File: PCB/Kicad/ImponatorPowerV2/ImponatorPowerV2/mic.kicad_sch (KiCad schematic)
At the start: 13 parts, among them U5 MAX4466EXK+T

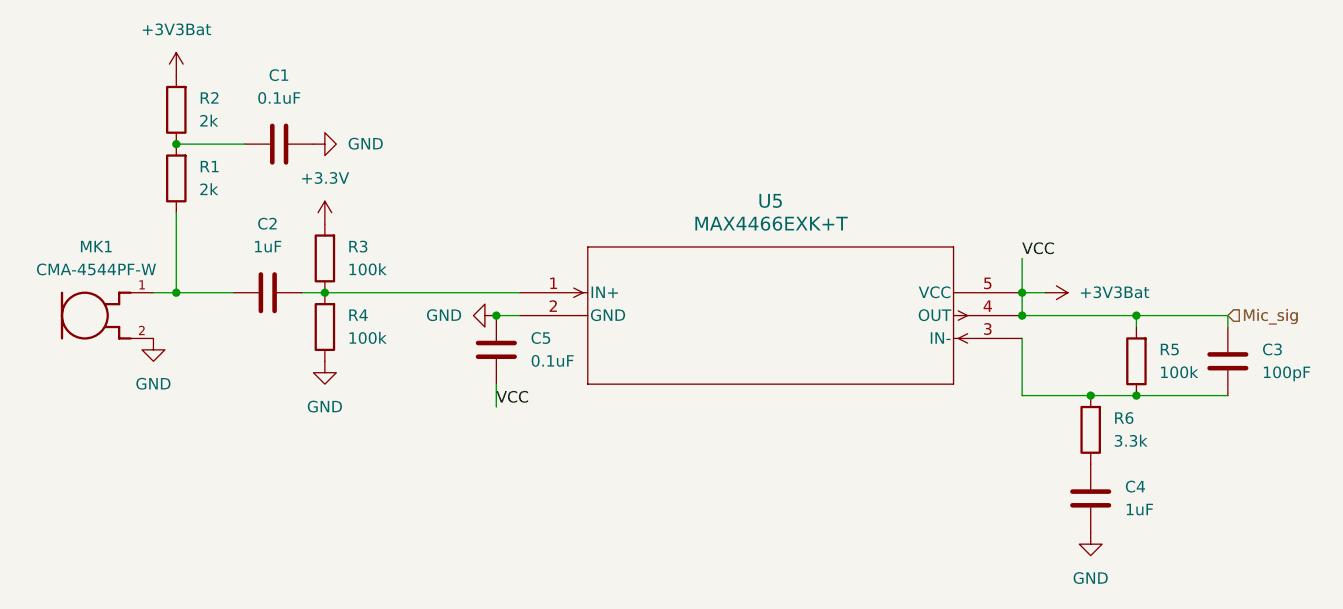
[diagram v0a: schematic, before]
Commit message: PCB routed, not ready for production
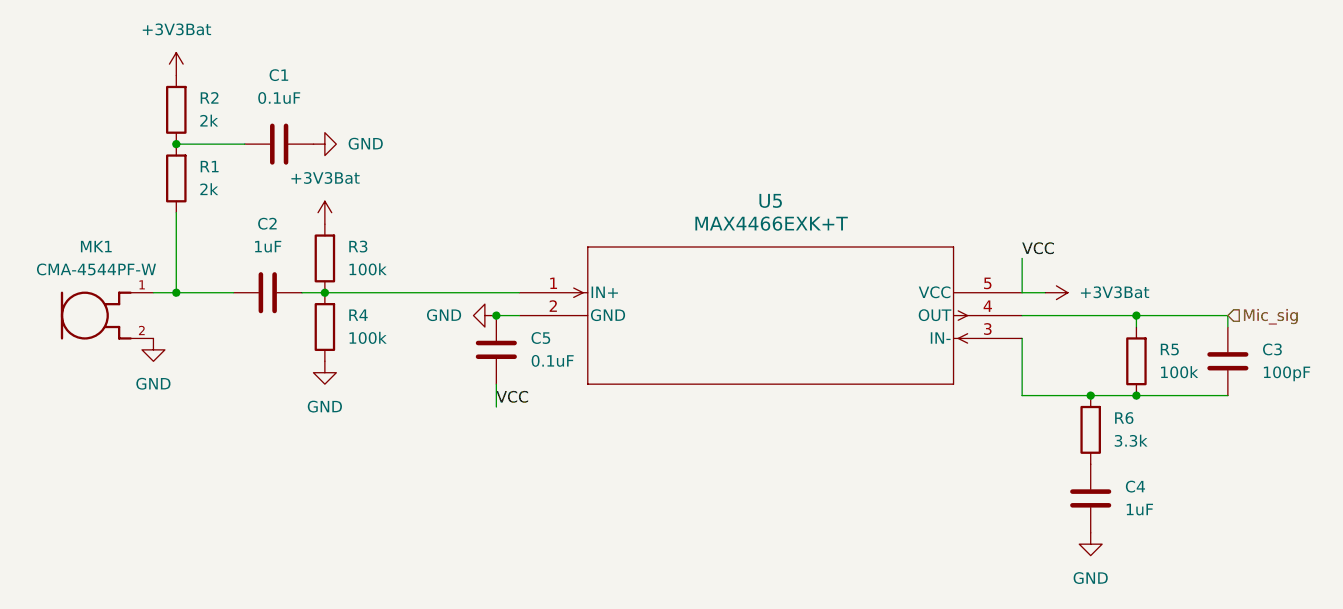
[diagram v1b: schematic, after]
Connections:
- net +3.3V is gone; now on net +3V3Bat: R3.2
- net +3V3Bat: no longer C3.1, R5.2, U5.4 (OUT)
- new net Mic_sig: C3.1, R5.2, U5.4 (OUT)
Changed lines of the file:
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@@
 	(paper "A4")
 	(junction
-		(at 154.94 87.63)
+		(at 167.64 90.17)
 		(diameter 0)
 		(color 0 0 0 0)
@@
 	)
 	(junction
-		(at 167.64 90.17)
-		(diameter 0)
-		(color 0 0 0 0)
-	)
-	(junction
 		(at 60.96 87.63)
 		(diameter 0)
@@
 	)
 	(junction
-		(at 154.94 90.17)
-		(diameter 0)
-		(color 0 0 0 0)
-	)
-	(junction
 		(at 167.64 99.06)
 		(diameter 0)
@@
 	(wire
 		(pts
+			(xy 154.94 90.17) (xy 167.64 90.17)
+		)
+		(stroke
+			(width 0)
+			(type default)
+		)
+	)
+	(wire
+		(pts
 			(xy 68.58 71.12) (xy 60.96 71.12)
 		)
@@
 	(wire
 		(pts
-			(xy 154.94 90.17) (xy 167.64 90.17)
-		)
-		(stroke
-			(width 0)
-			(type default)
-		)
-	)
-	(wire
-		(pts
 			(xy 167.64 90.17) (xy 167.64 91.44)
 		)
@@
 		(pts
 			(xy 60.96 87.63) (xy 60.96 78.74)
-		)
-		(stroke
-			(width 0)
-			(type default)
-		)
-	)
-	(wire
-		(pts
-			(xy 154.94 87.63) (xy 154.94 90.17)
 		)
 		(stroke
@@
 	)
 	(symbol
-		(lib_id "power:+3.3V")
+		(lib_id "power:GND")
+		(at 58.42 92.71 0)
+		(unit 1)
+		(exclude_from_sim no)
+		(in_bom yes)
+		(on_board yes)
+		(dnp no)
+		(fields_autoplaced yes)
+		(property "Reference" "#PWR01"
+			(at 58.42 99.06 0)
+			(effects
+				(font
+					(size 1.27 1.27)
+				)
+				(hide yes)
+			)
+		)
+		(property "Value" "GND"
+			(at 58.42 97.79 0)
+			(effects
+				(font
+					(size 1.27 1.27)
+				)
+			)
+		)
+		(property "Footprint" ""
+			(at 58.42 92.71 0)
+			(effects
+				(font
+					(size 1.27 1.27)
+				)
+				(hide yes)
+			)
+		)
+		(property "Datasheet" ""
+			(at 58.42 92.71 0)
+			(effects
+				(font
+					(size 1.27 1.27)
+				)
+				(hide yes)
+			)
+		)
+		(property "Description" "Power symbol creates a global label with name \"GND\" , ground"
+			(at 58.42 92.71 0)
+			(effects
+				(font
+					(size 1.27 1.27)
+				)
+				(hide yes)
+			)
+		)
+		(pin "1"
+		)
+		(instances
+			(project "ImponatorPowerV2"
+				(path "/39f9a456-0dc1-46da-8595-29035f4abc44/0165c1f8-8834-4f35-a624-6b8efab38fa5/a63d0856-d180-4795-9e0d-9fe5ece1cfcc"
+					(reference "#PWR01")
+					(unit 1)
+				)
+			)
+		)
+	)
+	(symbol
+		(lib_id "Device:R")
+		(at 162.56 102.87 180)
+		(unit 1)
+		(exclude_from_sim no)
+		(in_bom yes)
+		(on_board yes)
+		(dnp no)
+		(fields_autoplaced yes)
+		(property "Reference" "R6"
+			(at 165.1 101.5999 0)
+			(effects
+				(font
+					(size 1.27 1.27)
+				)
+				(justify right)
+			)
+		)
+		(property "Value" "3.3k"
+			(at 165.1 104.1399 0)
+			(effects
+				(font
+					(size 1.27 1.27)
+				)
+				(justify right)
+			)
+		)
+		(property "Footprint" "Resistor_SMD:R_0603_1608Metric"
+			(at 164.338 102.87 90)
+			(effects
+				(font
+					(size 1.27 1.27)
+				)
+				(hide yes)
+			)
+		)
+		(property "Datasheet" "~"
+			(at 162.56 102.87 0)
+			(effects
+				(font
+					(size 1.27 1.27)
+				)
+				(hide yes)
+			)
+		)
+		(property "Description" "Resistor"
+			(at 162.56 102.87 0)
+			(effects
+				(font
+					(size 1.27 1.27)
+				)
+				(hide yes)
+			)
+		)
+		(pin "2"
+		)
+		(pin "1"
+		)
+		(instances
+			(project "ImponatorPowerV2"
+				(path "/39f9a456-0dc1-46da-8595-29035f4abc44/0165c1f8-8834-4f35-a624-6b8efab38fa5/a63d0856-d180-4795-9e0d-9fe5ece1cfcc"
+					(reference "R6")
+					(unit 1)
+				)
+			)
+		)
+	)
+	(symbol
+		(lib_id "power:+3V3")
 		(at 77.47 80.01 0)
 		(unit 1)
@@
 			)
 		)
-		(property "Value" "+3.3V"
+		(property "Value" "+3V3Bat"
 			(at 77.47 74.93 0)
 			(effects
@@
 			)
 		)
-		(property "Description" "Power symbol creates a global label with name \"+3.3V\""
+		(property "Description" "Power symbol creates a global label with name \"+3V3\""
 			(at 77.47 80.01 0)
 			(effects
@@
 					(unit 1)
 				)
-			)
-		)
-	)
-	(symbol
-		(lib_id "power:GND")
-		(at 58.42 92.71 0)
-		(unit 1)
-		(exclude_from_sim no)
-		(in_bom yes)
-		(on_board yes)
-		(dnp no)
-		(fields_autoplaced yes)
-		(property "Reference" "#PWR01"
-			(at 58.42 99.06 0)
-			(effects
-				(font
-					(size 1.27 1.27)
-				)
-				(hide yes)
-			)
-		)
-		(property "Value" "GND"
-			(at 58.42 97.79 0)
-			(effects
-				(font
-					(size 1.27 1.27)
-				)
-			)
-		)
-		(property "Footprint" ""
-			(at 58.42 92.71 0)
-			(effects
-				(font
-					(size 1.27 1.27)
-				)
-				(hide yes)
-			)
-		)
-		(property "Datasheet" ""
-			(at 58.42 92.71 0)
-			(effects
-				(font
-					(size 1.27 1.27)
-				)
-				(hide yes)
-			)
-		)
-		(property "Description" "Power symbol creates a global label with name \"GND\" , ground"
-			(at 58.42 92.71 0)
-			(effects
-				(font
-					(size 1.27 1.27)
-				)
-				(hide yes)
-			)
-		)
-		(pin "1"
-		)
-		(instances
-			(project "ImponatorPowerV2"
-				(path "/39f9a456-0dc1-46da-8595-29035f4abc44/0165c1f8-8834-4f35-a624-6b8efab38fa5/a63d0856-d180-4795-9e0d-9fe5ece1cfcc"
-					(reference "#PWR01")
-					(unit 1)
-				)
-			)
-		)
-	)
-	(symbol
-		(lib_id "Device:R")
-		(at 162.56 102.87 180)
-		(unit 1)
-		(exclude_from_sim no)
-		(in_bom yes)
-		(on_board yes)
-		(dnp no)
-		(fields_autoplaced yes)
-		(property "Reference" "R6"
-			(at 165.1 101.5999 0)
-			(effects
-				(font
-					(size 1.27 1.27)
-				)
-				(justify right)
-			)
-		)
-		(property "Value" "3.3k"
-			(at 165.1 104.1399 0)
-			(effects
-				(font
-					(size 1.27 1.27)
-				)
-				(justify right)
-			)
-		)
-		(property "Footprint" "Resistor_SMD:R_0603_1608Metric"
-			(at 164.338 102.87 90)
-			(effects
-				(font
-					(size 1.27 1.27)
-				)
-				(hide yes)
-			)
-		)
-		(property "Datasheet" "~"
-			(at 162.56 102.87 0)
-			(effects
-				(font
-					(size 1.27 1.27)
-				)
-				(hide yes)
-			)
-		)
-		(property "Description" "Resistor"
-			(at 162.56 102.87 0)
-			(effects
-				(font
-					(size 1.27 1.27)
-				)
-				(hide yes)
-			)
-		)
-		(pin "2"
-		)
-		(pin "1"
-		)
-		(instances
-			(project "ImponatorPowerV2"
-				(path "/39f9a456-0dc1-46da-8595-29035f4abc44/0165c1f8-8834-4f35-a624-6b8efab38fa5/a63d0856-d180-4795-9e0d-9fe5ece1cfcc"
-					(reference "R6")
-					(unit 1)
-				)
